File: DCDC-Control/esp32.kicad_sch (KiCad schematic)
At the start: 7 parts, among them U1 ESP32-S3-MINI-1

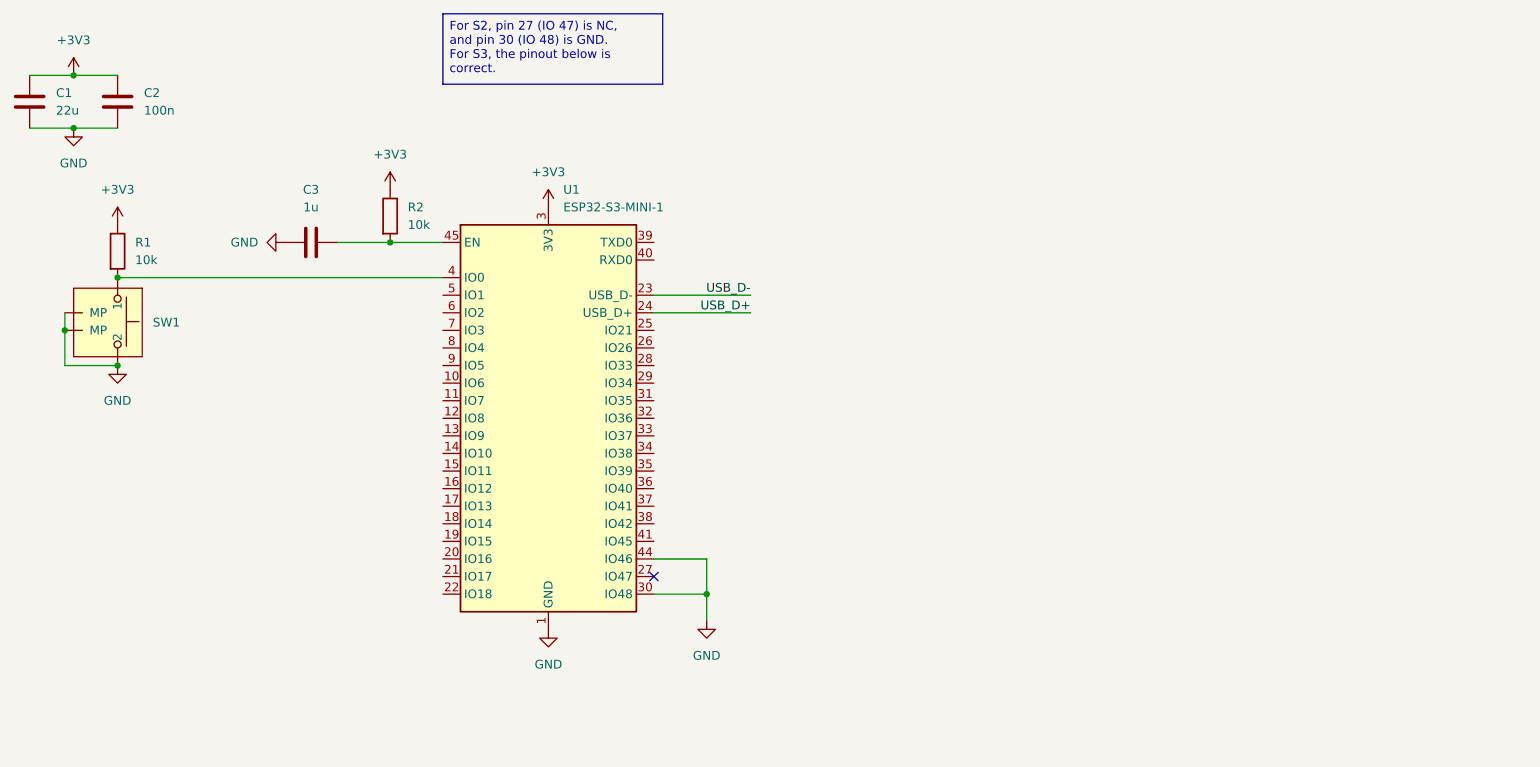
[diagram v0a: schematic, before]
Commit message: almost finished control schematics
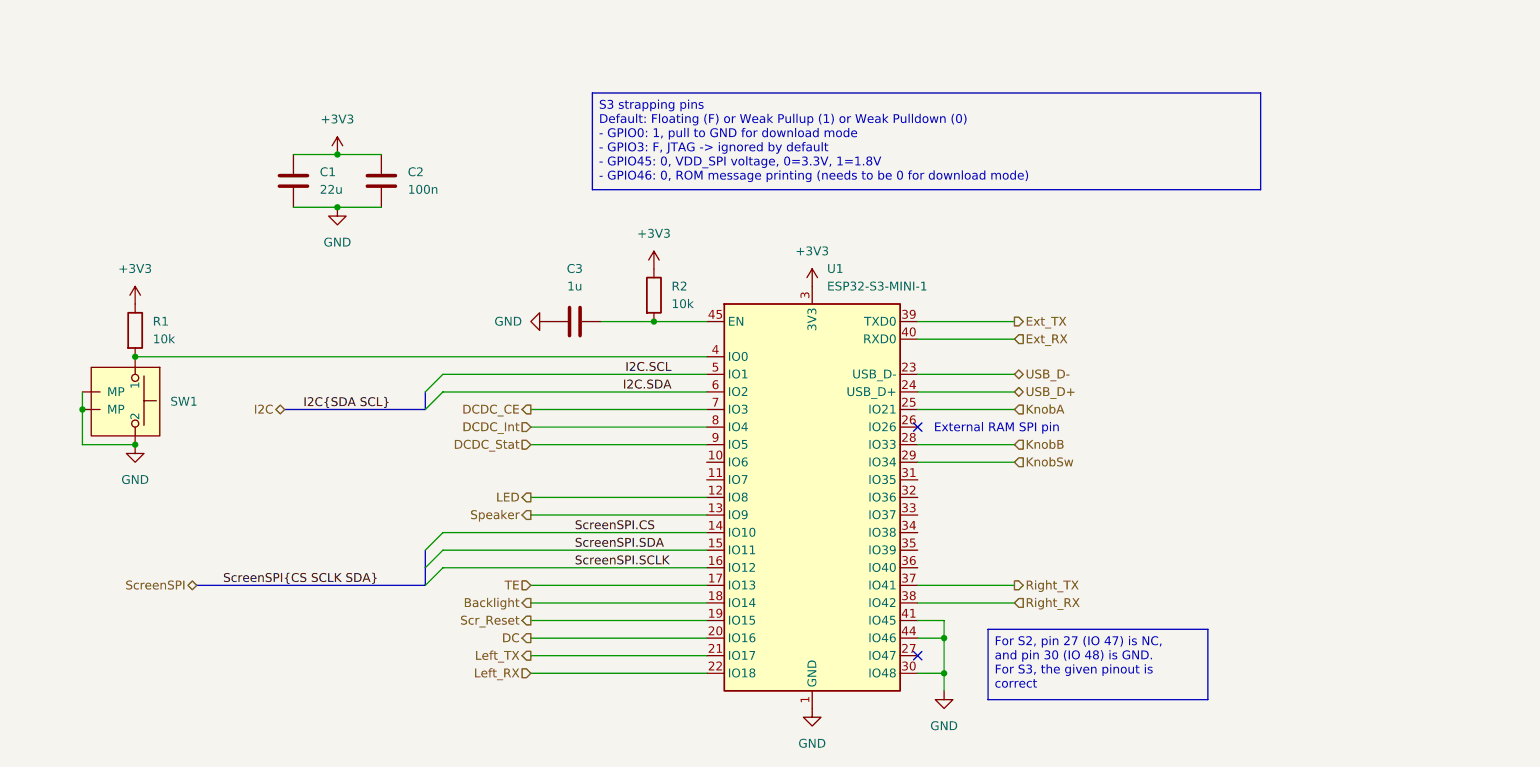
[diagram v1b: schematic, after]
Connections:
- net GND: now also U1.41 (IO45)
- net LED: now reaches U1.12 (IO8)
- net Speaker: now reaches U1.13 (IO9)
- net ScreenSPI.CS: now reaches U1.14 (IO10)
- net ScreenSPI.SDA: now reaches U1.15 (IO11)
- net ScreenSPI.SCLK: now reaches U1.16 (IO12)
- net TE: now reaches U1.17 (IO13)
- net Backlight: now reaches U1.18 (IO14)
- net Scr_Reset: now reaches U1.19 (IO15)
- net DC: now reaches U1.20 (IO16)
- net Left_TX: now reaches U1.21 (IO17)
- net Left_RX: now reaches U1.22 (IO18)
- net KnobA: now reaches U1.25 (IO21)
- net KnobB: now reaches U1.28 (IO33)
- net KnobSw: now reaches U1.29 (IO34)
- net Right_TX: now reaches U1.37 (IO41)
- net Right_RX: now reaches U1.38 (IO42)
- net Ext_TX: now reaches U1.39 (TXD0)
- net Ext_RX: now reaches U1.40 (RXD0)
- net I2C.SCL: now reaches U1.5 (IO1)
- net I2C.SDA: now reaches U1.6 (IO2)
- net DCDC_CE: now reaches U1.7 (IO3)
- net DCDC_Int: now reaches U1.8 (IO4)
- net DCDC_Stat: now reaches U1.9 (IO5)
- no-connect marks 1 -> 2
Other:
- note added: "External RAM SPI pin"
- moved on the sheet: C1, C2, C3, R1, R2, SW1

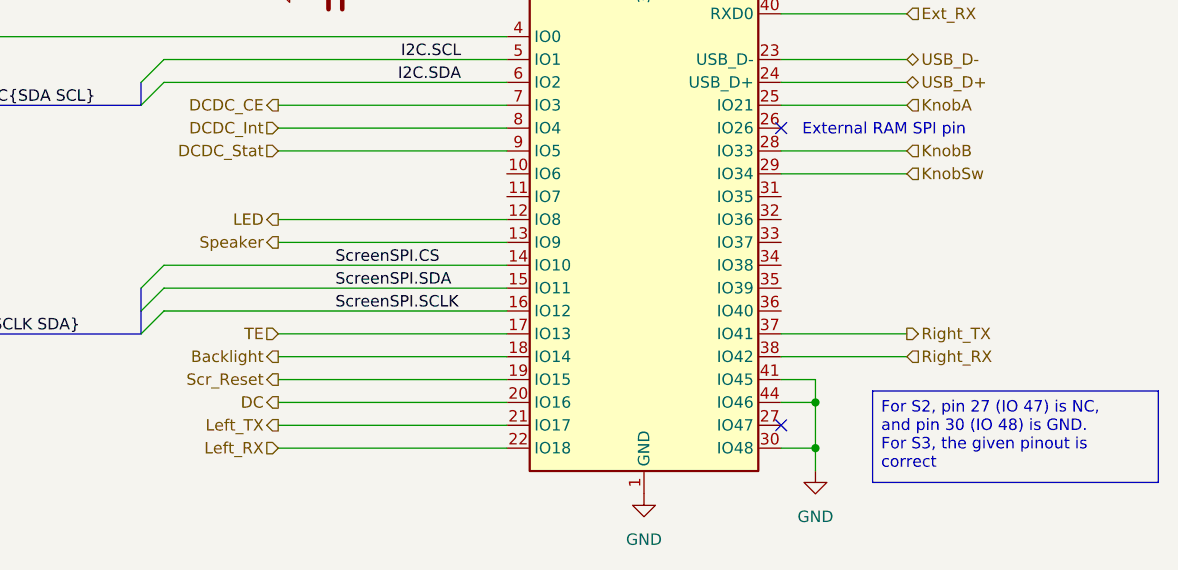
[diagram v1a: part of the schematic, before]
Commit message: some DCDC schematics
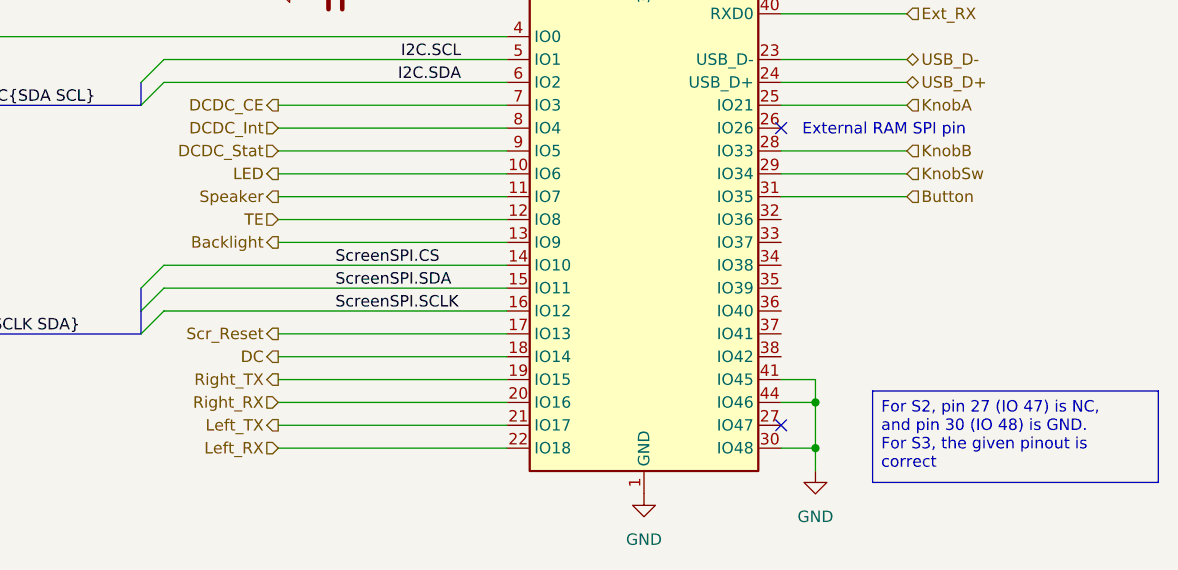
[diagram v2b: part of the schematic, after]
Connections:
- net Backlight: now also U1.13 (IO9); no longer U1.18 (IO14)
- net DC: now also U1.18 (IO14); no longer U1.20 (IO16)
- net LED: now also U1.10 (IO6); no longer U1.12 (IO8)
- net Right_RX: now also U1.20 (IO16); no longer U1.38 (IO42)
- net Right_TX: now also U1.19 (IO15); no longer U1.37 (IO41)
- net Scr_Reset: now also U1.17 (IO13); no longer U1.19 (IO15)
- net Speaker: now also U1.11 (IO7); no longer U1.13 (IO9)
- net TE: now also U1.12 (IO8); no longer U1.17 (IO13)
- net Button: now reaches U1.31 (IO35)

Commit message: wip
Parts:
- added R10, R9: 6.8k, Resistor_SMD:R_0603_1608Metric, symbol Device:R
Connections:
- net +3V3: now also R10.1, R9.1
- net I2C.SCL: now also R9.2
- net I2C.SDA: now also R10.2
